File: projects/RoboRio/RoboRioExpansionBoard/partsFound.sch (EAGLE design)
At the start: 11 parts, among them IC1 LM1086, IC2 24LC256P, IC3 40109

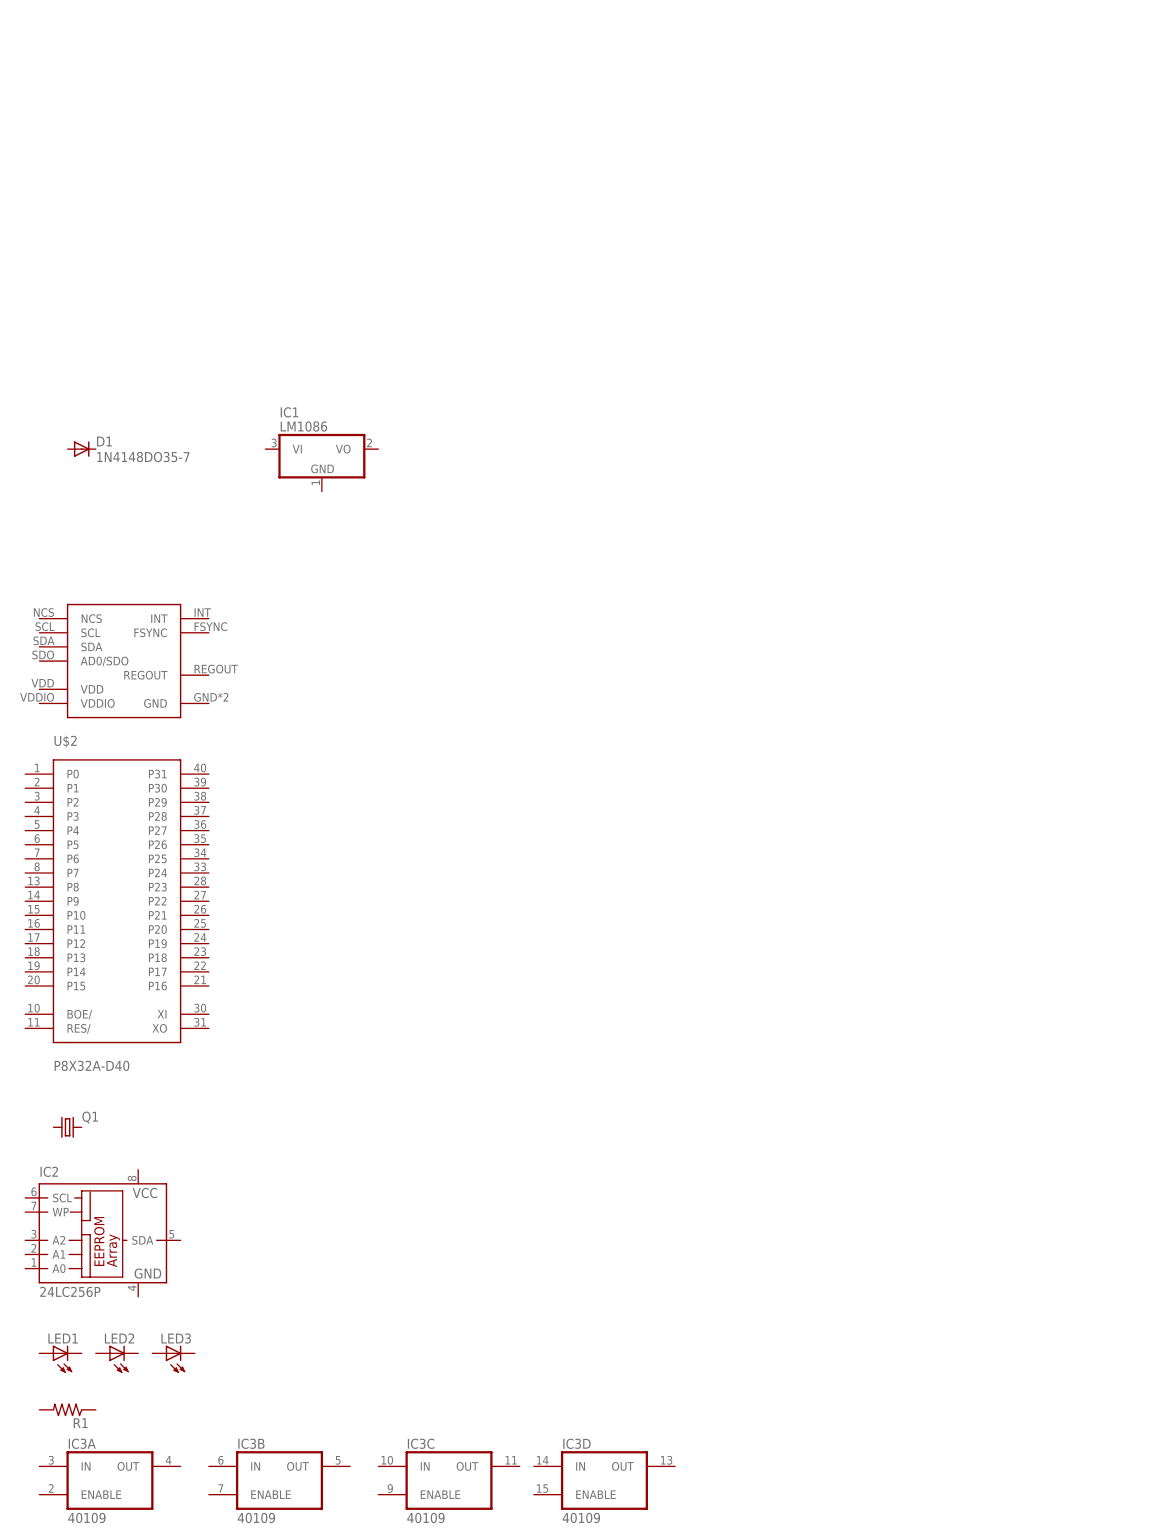
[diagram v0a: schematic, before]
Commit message: Added lowpass filters to adc inputs
(Without reverting Mr Emge’s work this time)
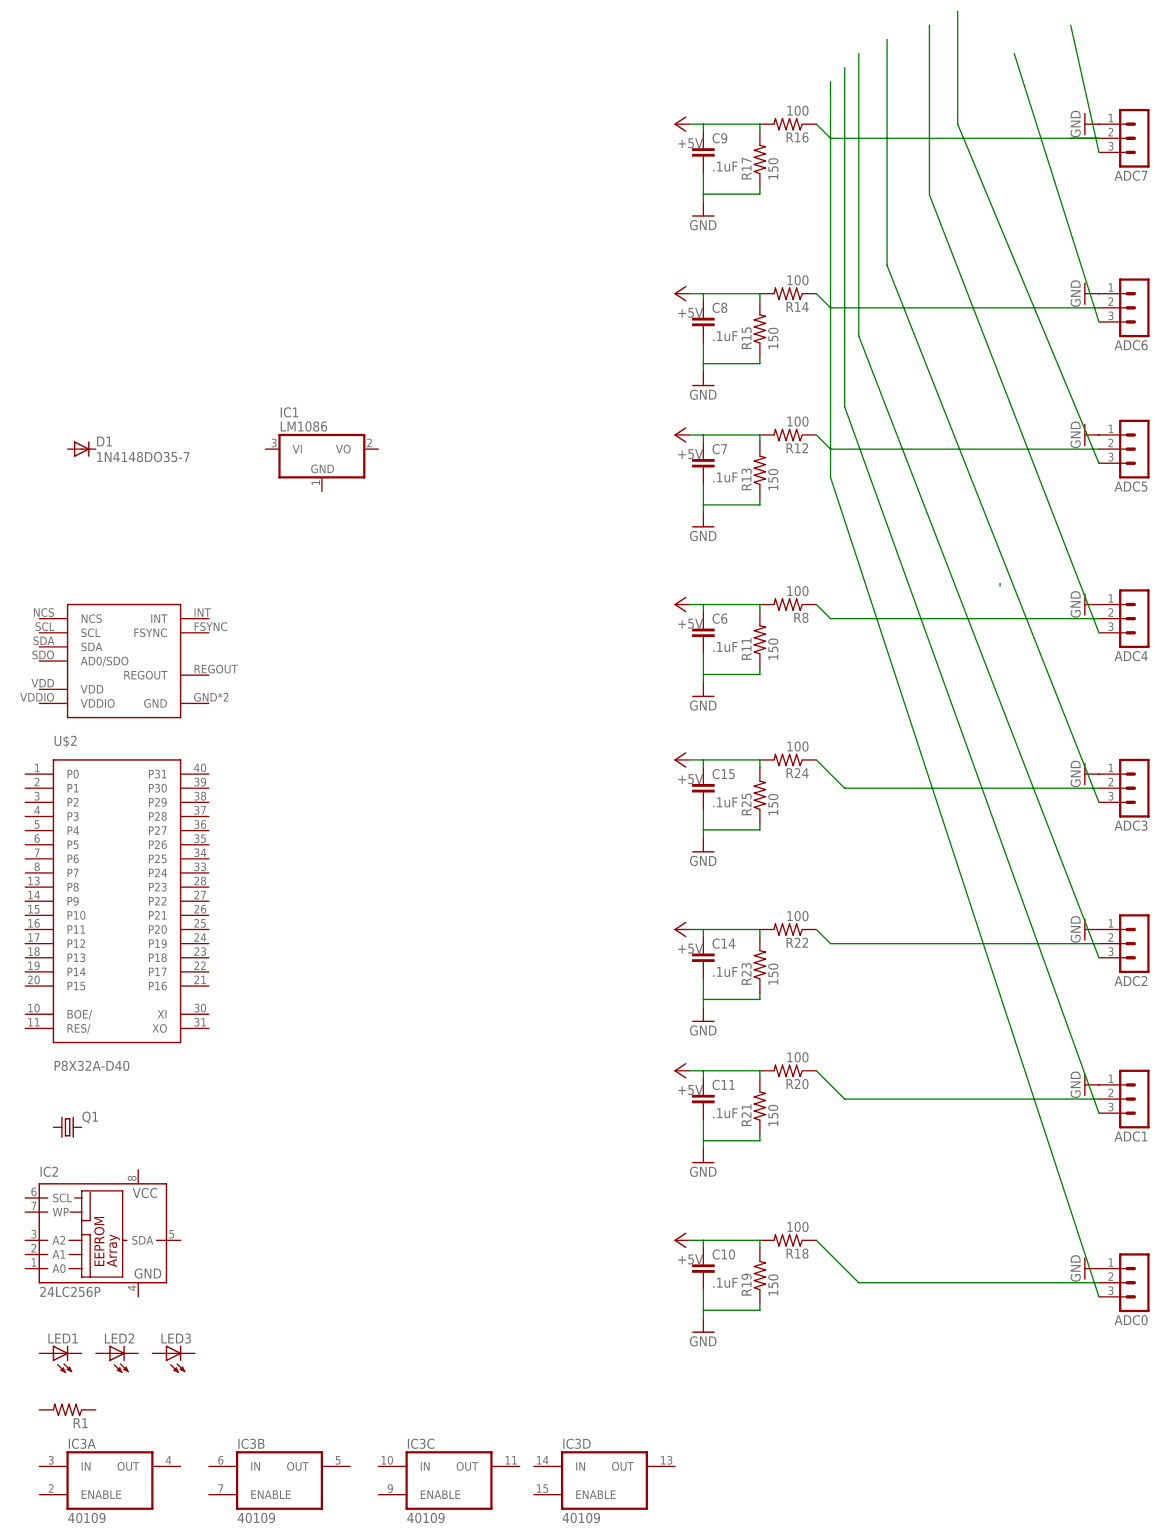
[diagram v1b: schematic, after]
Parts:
- added ADC0, ADC1, ADC2, ADC3, ADC4, ADC5, ADC6, ADC7: (no value), con-lstb-modified:MA03-1
- added C10, C11, C14, C15, C6, C7, C8, C9: .1uF, capacitor-wima:C7.5/6
- added R11, R13, R15, R17, R19, R21, R23, R25: 150, resistor:R-US_0309/V
- added R12, R14, R16, R18, R20, R22, R24, R8: 100, resistor:R-US_0309/V
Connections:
- new net +5V: C10.1, C11.1, C14.1, C15.1, C6.1, C7.1, C8.1, C9.1, R11.2, R12.2, R13.2, R14.2, R15.2, R16.2, R17.2, R18.2, R19.2, R20.2, R21.2, R22.2, R23.2, R24.2, R25.2, R8.2
- new net GND: ADC0.1, ADC1.1, ADC2.1, ADC3.1, ADC4.1, ADC5.1, ADC6.1, ADC7.1, C10.2, C11.2, C14.2, C15.2, C6.2, C7.2, C8.2, C9.2, R11.1, R13.1, R15.1, R17.1, R19.1, R21.1, R23.1, R25.1
- new net N$10: ADC0.3
- new net N$25: ADC0.2, R18.1
- new net N$28: ADC1.2, R20.1
- new net N$29: ADC2.2, R22.1
- new net N$3: ADC7.2, R16.1
- new net N$30: ADC3.2, R24.1
- new net N$31: ADC4.2, R8.1
- new net N$32: ADC5.2, R12.1
- new net N$33: ADC6.2, R14.1
- new net N$34: ADC7.3
- new net N$4: ADC6.3
- new net N$5: ADC5.3
- new net N$6: ADC4.3
- new net N$7: ADC3.3
- new net N$8: ADC2.3
- new net N$9: ADC1.3
